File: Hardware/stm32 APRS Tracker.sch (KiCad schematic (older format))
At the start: 41 parts

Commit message: schaltplan weiter
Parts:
- added R? (x2): 4,7k, symbol R
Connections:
- no-connect marks 4 -> 5
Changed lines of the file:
@@
 EESchema Schematic File Version 2
-LIBS:Resonator_3pins
-LIBS:ph-modules
 LIBS:power
 LIBS:device
@@
 LIBS:contrib
 LIBS:valves
+LIBS:ph-modules
+LIBS:Resonator_3pins
 LIBS:prog_sockets
+LIBS:schaltwandler
 LIBS:w_microcontrollers
-LIBS:schaltwandler
 LIBS:stm32 APRS Tracker-cache
 EELAYER 25 0
@@
 encoding utf-8
 Sheet 1 2
-Title ""
-Date ""
-Rev ""
+Title "APRS-GPS-Tracker"
+Date "2015-07-02"
+Rev "0.1"
 Comp ""
 Comment1 ""
@@
 	1    0    0    -1
 $EndComp
-Text Label 5800 2250 1    60   ~ 0
+Text Label 5800 1700 3    60   ~ 0
 I2C2_SDA
-Text Label 5900 2250 1    60   ~ 0
+Text Label 5900 1700 3    60   ~ 0
 I2C2_SCL
 Wire Wire Line
@@
 Text Notes 10050 2600 0    60   ~ 0
 Ausgang-\nAnpassung\n(Trafo)
+NoConn ~ 2550 4450
+$Comp
+L R R?
+U 1 1 5595D5C9
+P 5650 2250
+F 0 "R?" V 5730 2250 50  0000 C CNN
+F 1 "4,7k" V 5650 2250 50  0000 C CNN
+F 2 "" V 5580 2250 30  0000 C CNN
+F 3 "" H 5650 2250 30  0000 C CNN
+	1    5650 2250
+	0    1    1    0
+$EndComp
+$Comp
+L R R?
+U 1 1 5595D82C
+P 6050 2250
+F 0 "R?" V 6130 2250 50  0000 C CNN
+F 1 "4,7k" V 6050 2250 50  0000 C CNN
+F 2 "" V 5980 2250 30  0000 C CNN
+F 3 "" H 6050 2250 30  0000 C CNN
+	1    6050 2250
+	0    1    1    0
+$EndComp
+$Comp
+L +3.3V #PWR?
+U 1 1 5595D8DB
+P 5500 2250
+F 0 "#PWR?" H 5500 2100 50  0001 C CNN
+F 1 "+3.3V" H 5500 2390 50  0000 C CNN
+F 2 "" H 5500 2250 60  0000 C CNN
+F 3 "" H 5500 2250 60  0000 C CNN
+	1    5500 2250
+	0    -1   -1   0
+$EndComp
+$Comp
+L +3.3V #PWR?
+U 1 1 5595D967
+P 6200 2250
+F 0 "#PWR?" H 6200 2100 50  0001 C CNN
+F 1 "+3.3V" H 6200 2390 50  0000 C CNN
+F 2 "" H 6200 2250 60  0000 C CNN
+F 3 "" H 6200 2250 60  0000 C CNN
+	1    6200 2250
+	0    1    1    0
+$EndComp
 $EndSCHEMATC

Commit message: es ist wohl ein größerer stm32 nötig. mit mehr pins.
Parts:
- removed C?: 100n, Capacitors_SMD:C_0603, symbol C
- removed D?: red_txpwr_high, LEDs:LED-0603, symbol LED
- removed D?: orange_txpwr_low, LEDs:LED-0603, symbol LED
- removed D?: grün_GPS_lock, LEDs:LED-0603, symbol LED
- removed P?: CONN_01X04, symbol CONN_01X04
- removed R? (x3): 220, symbol R
- removed U? (x4): 74LS126, symbol 74LS126
- added BT101: CR2032, symbol Battery
- added C101: 22u, Capacitors_SMD:C_0805, symbol C
- added C112: 100n, Capacitors_SMD:C_0603, symbol C
- added P102: CONN_01X05, symbol CONN_01X05
- added R101: 1k, Resistors_SMD:R_0603, symbol R
- added R110, R111, R112: 1k, symbol R
- added R117: 390, Resistors_SMD:R_0603, symbol R
- added SW101: SW_TxPwr, symbol SW_PUSH
- added Y102: 32,768, symbol Crystal_Small
- R103, R107: renamed from R?; value 4,7k -> 1k
- gave numbers to parts that had none: 29
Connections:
- net labels added: +BATT, ClkSyncIn, DAC1, I2C1_SCL, I2C1_SDA, LCD_CS, LCD_D0, LCD_D1, LCD_D2, LCD_D3, LCD_D4, LCD_D5, LCD_D6, LCD_D7, LCD_RD, LCD_RS, LCD_Rst, LCD_WR, SD_CS, SD_~ON, SPI1_MISO, SPI1_MOSI, SPI1_SCK, Squelch, Tast0, uart3rx, uart3tx, ws2812
- net labels removed: I2C2_SCL, I2C2_SDA, PB0, PB1, PB2, PB3, analogOut
- wire segments 79 -> 114
- no-connect marks 5 -> 6
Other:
- note added: "Boot from FLASHROM"
- note added: "LCD"
- note added: "STM32F071CB 256k Flash\n4 UARTs!!"
- note added: "Sinnvolle Verwendung der seriellen Schnittstellen:\nI2C1: TempSensor LM75\nSPI1: SD-Karte\nUART1: 2m-Funkmodul\nUART2: Debug-Stecker\nUART3: GPS input\n8 Bit Parallel: LCD"
- note added: "TODOs\n\nI2C-LM75-Tempsensor"
- note added: "TPF 4,1kHz"
- note added: "neuer STM:\n35: VSS\n36: VDDio"
- note removed: "STM32F030C8T6 64k Flash\n"
- note removed: "TODOs\n\nI2C-OLED\nI2C-LM75-Tempsensor\nKnopf für TXPWR high/low"
- moved on the sheet: C102, C103, C104, C105, C106, C107, C108, D104, P101, R103, R107, R108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

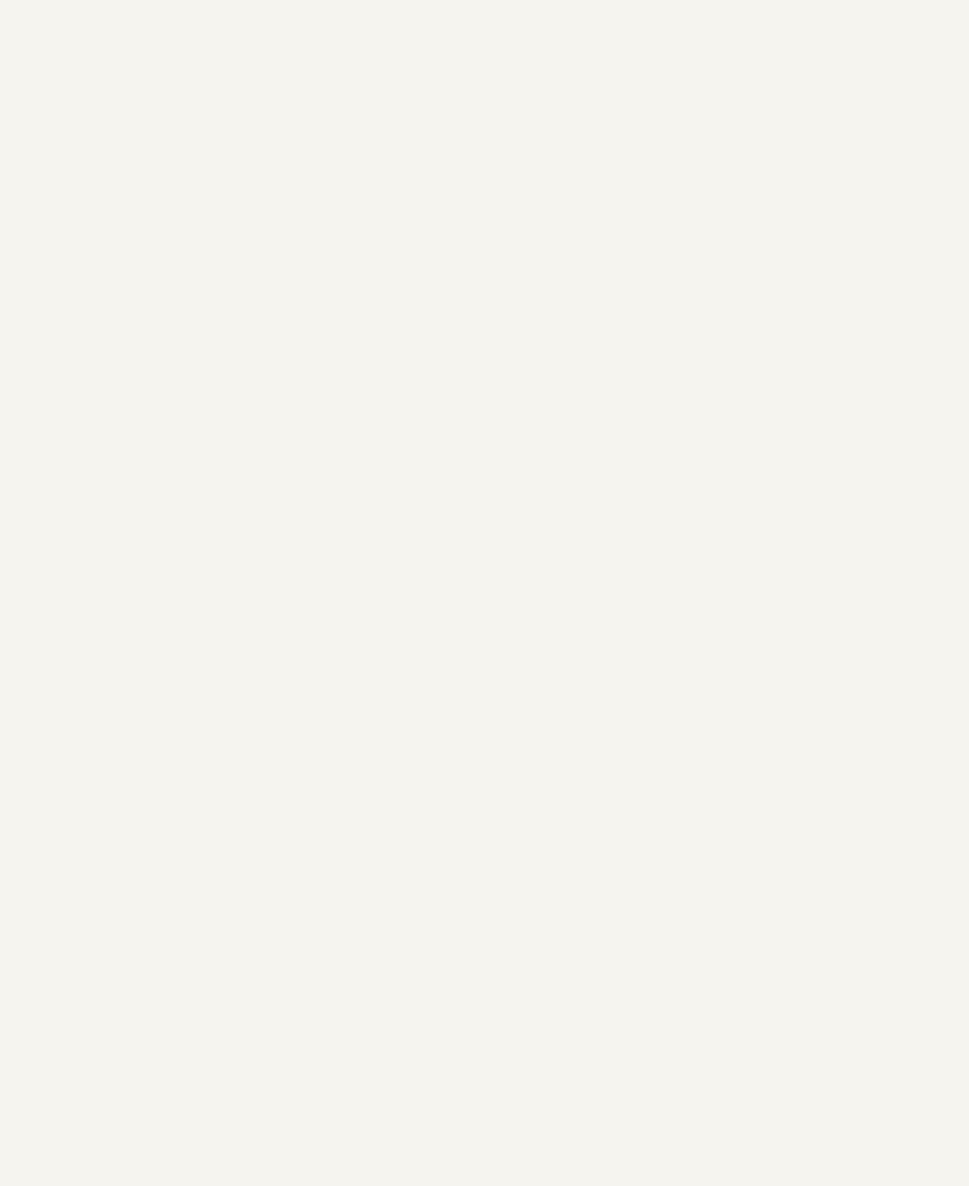
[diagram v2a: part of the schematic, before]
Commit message: Hinzufügen des STM32F103 (Entwurf)
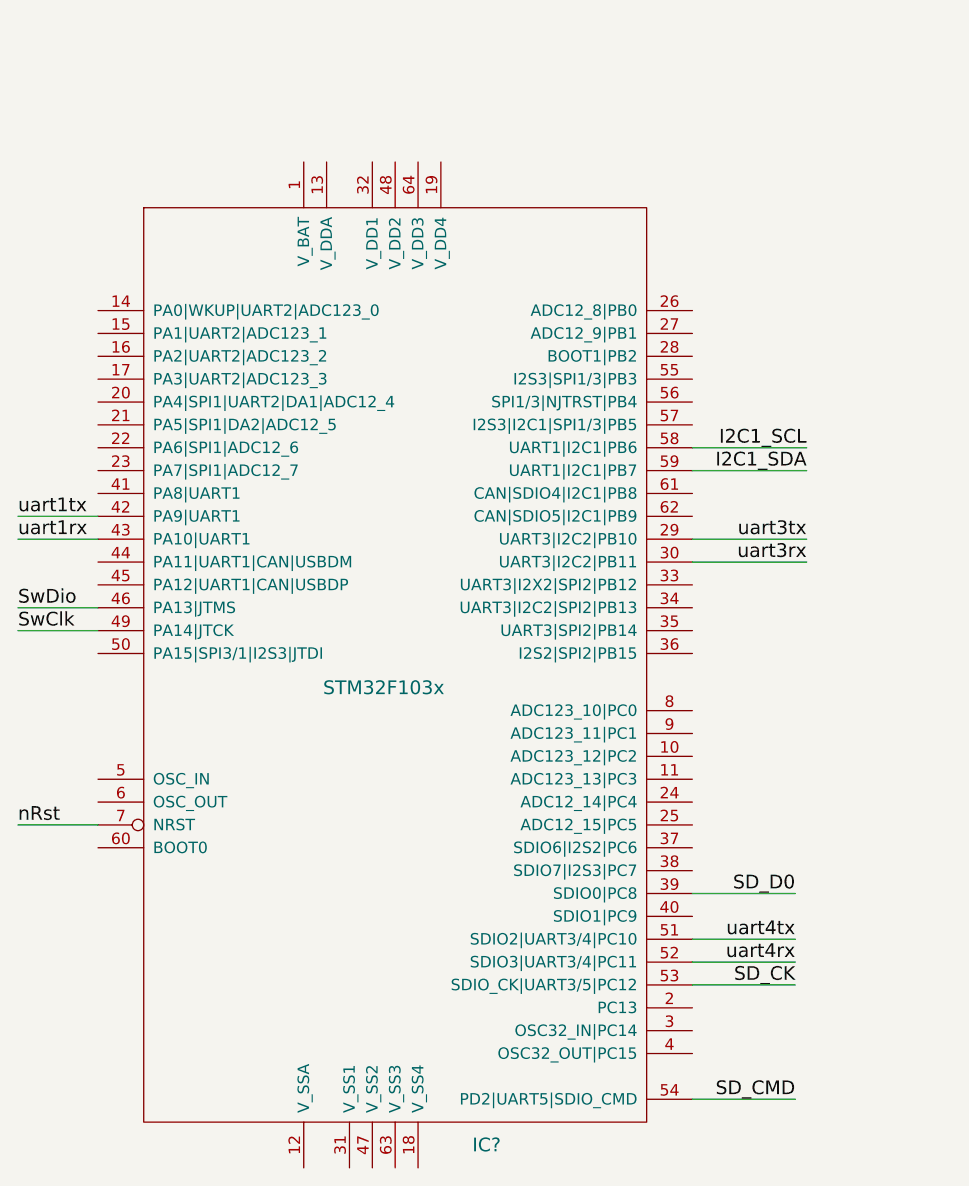
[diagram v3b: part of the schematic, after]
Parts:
- added IC?: STM32F103x, symbol STM32F103x
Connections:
- net GPS_RX: now also IC?.29 (UART3|I2C2|PB10)
- net GPS_TX: now also IC?.30 (UART3|I2C2|PB11)
- net I2C1_SCL: now also IC?.58 (UART1|I2C1|PB6)
- net I2C1_SDA: now also IC?.59 (UART1|I2C1|PB7)
- net SwClk: now also IC?.49 (PA14|JTCK)
- net SwDio: now also IC?.46 (PA13|JTMS)
- net nRst: now also IC?.7 (NRST)
- net uart1rx: now also IC?.43 (PA10|UART1)
- net uart1tx: now also IC?.42 (PA9|UART1)
- new net SD_CK: IC?.53 (SDIO_CK|UART3/5|PC12)
- new net SD_CMD: IC?.54 (PD2|UART5|SDIO_CMD)
- new net SD_D0: IC?.39 (SDIO0|PC8)
- new net uart4rx: IC?.52 (SDIO3|UART3/4|PC11)
- new net uart4tx: IC?.51 (SDIO2|UART3/4|PC10)
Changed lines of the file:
@@
 LIBS:contrib
 LIBS:valves
+LIBS:ph-modules
 LIBS:Resonator_3pins
+LIBS:prog_sockets
+LIBS:schaltwandler
+LIBS:w_microcontrollers
 LIBS:stm32 APRS Tracker-cache
 EELAYER 25 0
@@
 Wire Wire Line
 	5000 5600 4450 5600
+$Comp
+L STM32F103x IC?
+U 1 1 55A2E6F0
+P -2100 6250
+F 0 "IC?" H -1650 4200 60  0000 C CNN
+F 1 "STM32F103x" H -2100 6200 60  0000 C CNN
+F 2 "" H -1800 3600 60  0000 C CNN
+F 3 "" H -1800 3600 60  0000 C CNN
+	1    -2100 6250
+	1    0    0    -1
+$EndComp
+Text Label -3700 5950 0    60   ~ 0
+SwDio
+Text Label -3700 6050 0    60   ~ 0
+SwClk
+Wire Wire Line
+	-3350 6050 -3700 6050
+Wire Wire Line
+	-3700 5950 -3350 5950
+Text Label -3700 6900 0    60   ~ 0
+nRst
+Wire Wire Line
+	-3350 6900 -3700 6900
+Text Label -250 5350 2    60   ~ 0
+I2C1_SDA
+Text Label -250 5250 2    60   ~ 0
+I2C1_SCL
+Wire Wire Line
+	-750 5350 -250 5350
+Wire Wire Line
+	-250 5250 -750 5250
+Text Label -250 5750 2    60   ~ 0
+uart3rx
+Text Label -250 5650 2    60   ~ 0
+uart3tx
+Wire Wire Line
+	-250 5750 -750 5750
+Wire Wire Line
+	-750 5650 -250 5650
+Text Label -3700 5650 0    60   ~ 0
+uart1rx
+Text Label -3700 5550 0    60   ~ 0
+uart1tx
+Wire Wire Line
+	-3350 5650 -3700 5650
+Wire Wire Line
+	-3700 5550 -3350 5550
+Text Label -300 7400 2    60   ~ 0
+uart4tx
+Text Label -300 7500 2    60   ~ 0
+uart4rx
+Wire Wire Line
+	-300 7400 -750 7400
+Wire Wire Line
+	-750 7500 -300 7500
+Text Label -300 7200 2    60   ~ 0
+SD_D0
+Text Label -300 7600 2    60   ~ 0
+SD_CK
+Text Label -300 8100 2    60   ~ 0
+SD_CMD
+Wire Wire Line
+	-300 8100 -750 8100
+Wire Wire Line
+	-300 7200 -750 7200
+Wire Wire Line
+	-300 7600 -750 7600
 $EndSCHEMATC

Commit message: umbau auf massiv größeren STM fast abgeschlossen.
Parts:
- removed U102: STM32F030x4/6/8, LQFP48, symbol STM32F030x4/6/8
- added C? (x5): 100n, Capacitors_SMD:C_0603, symbol C
- added C?: 22u, Capacitors_SMD:C_0805, symbol C
- added D?: bt540, symbol D_Schottky
- added D?: LED, symbol LED
- added D?: 1n4148, symbol D
- added D?: 3,6V, symbol ZENER
- added F?: 500mA, symbol F_Small
- added P?: USB_B, symbol USB_B
- added R?: 220, symbol R
- added R? (x6): R, symbol R
- added U?: AP1117D33, symbol AP1117D33
- gave numbers to parts that had none: 1
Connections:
- net +3V3: now also C103.2, IC1.19 (V_DD4), IC1.32 (V_DD1), IC1.48 (V_DD2), IC1.64 (V_DD3), C?.1, D?.2 (A), R?.1, U?.2 (VO); no longer C103.1
- net +BATT: now also IC1.1 (V_BAT)
- net DAC1: now also IC1.20 (PA4|SPI1|UART2|DA1|ADC12_4)
- net GND: now also C103.1, IC1.18 (V_SS4), IC1.31 (V_SS1), IC1.47 (V_SS2), IC1.63 (V_SS3), R101.1, C?.1, C?.2, C?.2, P?.4 (GND), R?.2, U?.1 (GND/ADJ); no longer C103.2, R101.2
- net I2C1_SCL: now also IC1.61 (CAN|SDIO4|I2C1|PB8); no longer IC1.58 (UART1|I2C1|PB6)
- net I2C1_SDA: now also IC1.62 (CAN|SDIO5|I2C1|PB9); no longer IC1.59 (UART1|I2C1|PB7)
- net LCD_D0: now also IC1.26 (ADC12_8|PB0)
- net LCD_D1: now also IC1.27 (ADC12_9|PB1)
- net LCD_D2: now also IC1.28 (BOOT1|PB2)
- net LCD_D3: now also IC1.55 (I2S3|SPI1/3|PB3)
- net LCD_D4: now also IC1.56 (SPI1/3|NJTRST|PB4)
- net LCD_D5: now also IC1.57 (I2S3|I2C1|SPI1/3|PB5)
- net LCD_D6: now also IC1.58 (UART1|I2C1|PB6)
- net LCD_D7: now also IC1.59 (UART1|I2C1|PB7)
- net PTT: now also IC1.14 (PA0|WKUP|UART2|ADC123_0)
- net SD_~ON: now also IC1.35 (UART3|SPI2|PB14)
- net SPI1_MISO: now also IC1.22 (PA6|SPI1|ADC12_6)
- net SPI1_MOSI: now also IC1.23 (PA7|SPI1|ADC12_7)
- net SPI1_SCK: now also IC1.21 (PA5|SPI1|DA2|ADC12_5)
- net Squelch: now also IC1.50 (PA15|SPI3/1|I2S3|JTDI)
- net TXPower: now also IC1.8 (ADC123_10|PC0)
- net Tast0: now also IC1.36 (I2S2|SPI2|PB15)
- net VAA: now also IC1.13 (V_DDA)
- net analogIn: now also IC1.15 (PA1|UART2|ADC123_1)
- net uart2rx: now also IC1.17 (PA3|UART2|ADC123_3)
- net uart2tx: now also IC1.16 (PA2|UART2|ADC123_2)
- net ws2812: now also IC1.33 (UART3|I2X2|SPI2|PB12)
- net HfPowerDown: now reaches DRA101.6 (PowerDown)
- net HfPowerDown: now also IC1.9 (ADC123_11|PC1)
- net at Y102.1: now also IC1.3 (OSC32_IN|PC14)
- net at Y102.2: now also IC1.4 (OSC32_OUT|PC15)
- net at Y101.1: now also IC1.5 (OSC_IN)
- net at Y101.3: now also IC1.6 (OSC_OUT)
- net U_Akku: now reaches IC1.10 (ADC123_12|PC2)
- net U_Akku: now also C?.1, R?.1, R?.2
- net U_USB: now reaches IC1.11 (ADC123_13|PC3)
- net U_USB: now also C?.1, D?.1 (K), R?.1, R?.2
- net GNDA: now reaches IC1.12 (V_SSA)
- net GNDA: now also C?.2, C?.2, C?.2, D?.2 (A), R?.2, R?.2, R?.2
- net U_3,3V: now reaches IC1.24 (ADC12_14|PC4)
- net U_3,3V: now also C?.1, R?.1, R?.2
- net LED: now reaches IC1.34 (UART3|I2C2|SPI2|PB13)
- net at IC1.60 (BOOT0): now also R101.2
- new net: C?.1, C?.2, D?.1 (K), D?.1 (K), U?.3 (VI)
- new net: D?.2 (A), F?.1
- new net: D?.1 (K), R?.1
- new net +5V: D?.2 (A), F?.2, P?.1 (VCC), R?.1
- new net Akku: R?.1
- no-connect marks 6 -> 4
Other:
- note added: "USB EMI\nModule"
- note removed: "Boot from FLASHROM"
- note removed: "STM32F071CB 256k Flash\n4 UARTs!!"
- note removed: "TODOs\n\nI2C-LM75-Tempsensor"
- note removed: "neuer STM:\n35: VSS\n36: VDDio"
- moved on the sheet: BT101, C101, C102, C103, C104, C105, C106, C107, C108, C109, C110, C111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
